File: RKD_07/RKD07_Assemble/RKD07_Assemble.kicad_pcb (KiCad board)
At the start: 2 copper layers, 409.6 x 100 mm, 166 parts, among them J1 Conn_01x02_Socket, J10 Conn_01x04, J11 TRRS, J12 Conn_01x06, J13 Conn_01x06, J2 Conn_01x24, J3 Conn_01x24, J4 Conn_01x24, J5 Qwiic_RA, J6 Qwiic_RA, J7 Conn_01x06, J8 Conn_01x06, J9 Conn_01x04, M3 Mark, M4 Mark, M5 Mark, M6 Mark, M8 Mark, SW1 SW_Push, SW10 SW_Push, SW11 SW_Push, SW12 SW_Push, SW13 SW_Push, SW14 SW_Push, SW15 SW_Push, SW16 SW_Push, SW17 SW_Push, SW18 SW_Push, SW19 SW_Push, SW2 SW_Push, SW20 SW_Push, SW21 SW_Push, SW22 SW_Push, SW23 SW_Push, SW24 SW_Push, SW25 SW_Push, SW26 SW_Push, SW27 SW_Push, SW28 SW_Push, SW29 SW_Push, SW3 SW_Push, SW30 RotaryEncoder_Switch, SW31 SW_Push, SW4 SW_Push, SW5 SW_Push, SW51 SW_Push, SW52 SW_Push, SW53 SW_Push, SW54 SW_Push, SW55 SW_Push, SW56 SW_Push, SW57 SW_Push, SW58 SW_Push, SW59 SW_Push, SW6 SW_Push, SW60 SW_Push, SW61 SW_Push, SW62 SW_Push, SW63 SW_Push, SW64 SW_Push, SW65 SW_Push, SW66 SW_Push, SW67 SW_Push, SW68 SW_Push, SW69 SW_Push, SW7 SW_Push, SW70 SW_Push, SW71 SW_Push, SW72 SW_Push, SW73 SW_Push, SW74 SW_Push, SW75 SW_Push, SW76 SW_Push, SW77 SW_Push, SW78 SW_Push, SW79 SW_Push, SW8 SW_Push, SW80 SW_Push, SW81 SW_Push, SW82 SW_Push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

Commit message: ネジ穴見直し
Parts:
- moved SW31 1.19 mm to (166.7, 188.1)
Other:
- board size 409.6 x 100 mm -> 409.6 x 97.6 mm

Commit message: 07 I2C抵抗追加
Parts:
- removed Ref** (x2): Val**, kbd_Hole:m2_Spacer_Hole_hex
- added R3: R, Resistor_THT:R_Axial_DIN0207_L6.3mm_D2.5mm_P10.16mm_Horizontal, B.Cu at (173.1, 119.6)
- added R4: R, Resistor_THT:R_Axial_DIN0207_L6.3mm_D2.5mm_P10.16mm_Horizontal, B.Cu at (169.1, 119.6)
- SW25, SW4, SW86, SW88: footprint Rikkodo_FootPrint:rkd_Asm_ChocV2_Hotswap_2u -> Rikkodo_FootPrint:rkd_Asm_ChocV2_Hotswap_2uW
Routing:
- net 3v3_L: track 140.2 -> 173.1 mm
- net GND_L: track 241.2 -> 213.1 mm
- net SCL/TX_L: track 145.9 -> 140.4 mm, vias 0 -> 1
- net SCL/TX_R: track 188.9 -> 191.9 mm
- net SDA/SCK_L: track 152.5 -> 155.0 mm, vias 0 -> 1
- net VCC_L: track 23.0 -> 20.9 mm
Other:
- outline, holes or cut-outs redrawn
- board text added: "GND 3V3 SDA SCL"
- board text added: "GND SCK TX MOT CS 3V3"
- board text removed: "SCL/TX"
- board text removed: "SDA/SCK"

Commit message: 07 ワイヤ調整
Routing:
- net 3v3_R: track 254.2 -> 261.9 mm
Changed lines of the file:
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@@
 	(gr_arc
 		(start 248.840625 133.349908)
-		(mid 247.998809 133.001216)
+		(mid 247.998793 133.001225)
 		(end 247.650117 132.1594)
 		(stroke
@@
 	(gr_arc
 		(start 76.199975 94.05935)
-		(mid 76.548716 93.217466)
+		(mid 76.548713 93.217448)
 		(end 77.3906 92.868725)
 		(stroke
@@
 	(gr_arc
 		(start 70.246875 92.86875)
-		(mid 71.088796 93.217454)
+		(mid 71.088828 93.217436)
 		(end 71.4375 94.059375)
 		(stroke
@@
 	(gr_arc
 		(start 4.7625 94.059375)
-		(mid 5.111228 93.217485)
+		(mid 5.11123 93.21748)
 		(end 5.953125 92.86875)
 		(stroke
@@
 	(gr_arc
 		(start 251.209746 133.350138)
-		(mid 252.059665 133.694421)
+		(mid 252.059664 133.694427)
 		(end 252.412712 134.540738)
 		(stroke
@@
 	)
 	(segment
+		(start 256.579903 180.975152)
+		(end 256.579903 157.755547)
+		(width 0.25)
+		(layer "B.Cu")
+		(net 63)
+	)
+	(segment
 		(start 190.75 127.928125)
 		(end 190.75 117.859225)
@@
 	)
 	(segment
-		(start 238.125 186.928125)
-		(end 247.81249 186.928125)
+		(start 259.8042 154.53125)
+		(end 267.37812 154.53125)
 		(width 0.25)
 		(layer "B.Cu")
@@
 	)
 	(segment
-		(start 188.11875 165.80625)
-		(end 195.945625 173.633125)
+		(start 214.135375 186.751)
+		(end 224.177115 186.751)
 		(width 0.25)
 		(layer "B.Cu")
@@
 	)
 	(segment
-		(start 250.788898 183.951717)
-		(end 253.603338 183.951717)
+		(start 188.11875 165.80625)
+		(end 195.945625 173.633125)
 		(width 0.25)
 		(layer "B.Cu")
@@
 	)
 	(segment
-		(start 200.620481 178.91125)
-		(end 203.193606 181.484375)
+		(start 253.603338 183.951717)
+		(end 256.579903 180.975152)
+		(width 0.25)
+		(layer "B.Cu")
+		(net 63)
+	)
+	(segment
+		(start 224.177115 186.751)
+		(end 226.976398 183.951717)
 		(width 0.25)
 		(layer "B.Cu")
@@
 	)
 	(segment
-		(start 226.976398 183.951717)
-		(end 235.148592 183.951717)
+		(start 200.620481 178.91125)
+		(end 203.193606 181.484375)
 		(width 0.25)
 		(layer "B.Cu")
@@
 	)
 	(segment
-		(start 190.75 117.859225)
-		(end 195.249755 113.35947)
+		(start 211.18125 183.796875)
+		(end 214.135375 186.751)
 		(width 0.25)
 		(layer "B.Cu")
@@
 	)
 	(segment
-		(start 256.579903 180.975152)
-		(end 256.579903 157.755547)
+		(start 238.125 186.928125)
+		(end 247.81249 186.928125)
 		(width 0.25)
 		(layer "B.Cu")
@@
 	)
 	(segment
-		(start 203.193606 181.484375)
-		(end 210.740625 181.484375)
+		(start 190.75 117.859225)
+		(end 195.249755 113.35947)
 		(width 0.25)
 		(layer "B.Cu")
@@
 	)
 	(segment
-		(start 190.75 128.932544)
-		(end 190.75 127.928125)
+		(start 203.193606 181.484375)
+		(end 210.740625 181.484375)
 		(width 0.25)
 		(layer "B.Cu")
@@
 	)
 	(segment
-		(start 214.135375 186.751)
-		(end 224.177115 186.751)
+		(start 190.75 128.932544)
+		(end 190.75 127.928125)
 		(width 0.25)
 		(layer "B.Cu")
@@
 	)
 	(segment
-		(start 211.18125 183.796875)
-		(end 214.135375 186.751)
+		(start 247.81249 186.928125)
+		(end 250.788898 183.951717)
 		(width 0.25)
 		(layer "B.Cu")
@@
 	)
 	(segment
-		(start 259.8042 154.53125)
-		(end 267.37812 154.53125)
+		(start 226.976398 183.951717)
+		(end 235.148592 183.951717)
 		(width 0.25)
 		(layer "B.Cu")
@@
 	)
 	(segment
-		(start 247.81249 186.928125)
-		(end 250.788898 183.951717)
+		(start 250.788898 183.951717)
+		(end 253.603338 183.951717)
 		(width 0.25)
 		(layer "B.Cu")
@@
 	)
 	(segment
-		(start 224.177115 186.751)
-		(end 226.976398 183.951717)
-		(width 0.25)
-		(layer "B.Cu")
-		(net 63)
-	)
-	(segment
 		(start 195.945625 173.633125)
 		(end 197.28125 173.633125)
@@
 	)
 	(segment
-		(start 253.603338 183.951717)
-		(end 256.579903 180.975152)
-		(width 0.25)
-		(layer "B.Cu")
-		(net 63)
-	)
-	(segment
 		(start 373.85625 153.0062)
 		(end 392.90625 153.0062)
@@
 	)
 	(segment
-		(start 188.11875 163.80625)
-		(end 187.428125 163.80625)
+		(start 265.950756 175.77149)
+		(end 265.950756 166.813439)
 		(width 0.5)
 		(layer "B.Cu")
@@
 	)
 	(segment
-		(start 265.950756 175.77149)
-		(end 257.175216 184.54703)
-		(width 0.3)
+		(start 188.11875 163.80625)
+		(end 187.428125 163.80625)
+		(width 0.5)
 		(layer "B.Cu")
 		(net 69)
 	)
 	(segment
-		(start 193.464221 108.35947)
-		(end 197.579855 108.35947)
-		(width 0.3)
+		(start 207.44672 187.523595)
+		(end 225.121614 187.523595)
+		(width 0.5)
 		(layer "B.Cu")
 		(net 69)
 	)
 	(segment
-		(start 237.529887 188.11875)
-		(end 233.958167 184.54703)
-		(width 0.3)
+		(start 271.73112 156.13225)
+		(end 267.37812 156.13225)
+		(width 0.5)
 		(layer "B.Cu")
 		(net 69)
 	)
 	(segment
-		(start 252.0521 184.54703)
-		(end 248.48038 188.11875)
-		(width 0.3)
+		(start 251.22172 184.54703)
+		(end 257.175216 184.54703)
+		(width 0.5)
 		(layer "B.Cu")
 		(net 69)
 	)
 	(segment
-		(start 205.978125 186.055)
-		(end 207.44672 187.523595)
+		(start 237.529887 188.11875)
+		(end 247.65 188.11875)
 		(width 0.5)
 		(layer "B.Cu")
@@
 	)
 	(segment
-		(start 233.958167 184.54703)
-		(end 228.004879 184.54703)
+		(start 193.464221 108.35947)
+		(end 197.579855 108.35947)
 		(width 0.3)
 		(layer "B.Cu")
@@
 	)
 	(segment
-		(start 185.75 127.928125)
-		(end 185.75 157.776739)
-		(width 0.3)
+		(start 204.7875 186.055)
+		(end 205.978125 186.055)
+		(width 0.5)
 		(layer "B.Cu")
 		(net 69)
 	)
 	(segment
-		(start 228.004879 184.54703)
-		(end 225.028314 187.523595)
+		(start 185.75 127.928125)
+		(end 185.75 157.776739)
 		(width 0.3)
 		(layer "B.Cu")
@@
 	)
 	(segment
-		(start 204.7875 186.055)
-		(end 205.978125 186.055)
+		(start 234.085137 184.674)
+		(end 237.529887 188.11875)
 		(width 0.5)
 		(layer "B.Cu")
@@
 	)
 	(segment
-		(start 225.028314 187.523595)
-		(end 207.44672 187.523595)
-		(width 0.3)
+		(start 272.17912 163.071185)
+		(end 272.17912 156.58025)
+		(width 0.5)
 		(layer "B.Cu")
 		(net 69)
 	)
 	(segment
-		(start 187.428125 163.80625)
-		(end 185.7375 165.496875)
+		(start 265.950756 166.813439)
+		(end 267.838195 164.926)
 		(width 0.5)
 		(layer "B.Cu")
@@
 	)
 	(segment
-		(start 185.75 127.928125)
-		(end 185.75 116.073691)
-		(width 0.3)
+		(start 187.428125 163.80625)
+		(end 185.7375 165.496875)
+		(width 0.5)
 		(layer "B.Cu")
 		(net 69)
 	)
 	(segment
-		(start 265.98225 157.42712)
-		(end 265.98225 175.77149)
+		(start 185.75 127.928125)
+		(end 185.75 116.073691)
 		(width 0.3)
 		(layer "B.Cu")
@@
 	)
 	(segment
-		(start 185.75 157.776739)
-		(end 196.724511 168.75125)
-		(width 0.3)
+		(start 267.838195 164.926)
+		(end 270.324305 164.926)
+		(width 0.5)
 		(layer "B.Cu")
 		(net 69)
 	)
 	(segment
-		(start 257.175216 184.54703)
-		(end 252.0521 184.54703)
-		(width 0.3)
+		(start 225.121614 187.523595)
+		(end 227.971209 184.674)
+		(width 0.5)
 		(layer "B.Cu")
 		(net 69)
 	)
 	(segment
-		(start 248.48038 188.11875)
-		(end 237.529887 188.11875)
+		(start 185.75 157.776739)
+		(end 196.724511 168.75125)
 		(width 0.3)
 		(layer "B.Cu")
@@
 	)
 	(segment
-		(start 267.37812 156.03125)
-		(end 265.98225 157.42712)
-		(width 0.3)
-		(layer "B.Cu")
-		(net 69)
-	)
-	(segment
 		(start 197.28125 178.713125)
 		(end 197.28125 176.173125)
@@
 	)
 	(segment
-		(start 265.98225 175.77149)
+		(start 227.971209 184.674)
+		(end 234.085137 184.674)
+		(width 0.5)
+		(layer "B.Cu")
+		(net 69)
+	)
+	(segment
+		(start 205.978125 186.055)
+		(end 207.44672 187.523595)
+		(width 0.5)
+		(layer "B.Cu")
+		(net 69)
+	)
+	(segment
+		(start 247.65 188.11875)
+		(end 251.22172 184.54703)
+		(width 0.5)
+		(layer "B.Cu")
+		(net 69)
+	)
+	(segment
+		(start 257.175216 184.54703)
 		(end 265.950756 175.77149)
-		(width 0.3)
+		(width 0.5)
+		(layer "B.Cu")
+		(net 69)
+	)
+	(segment
+		(start 270.324305 164.926)
+		(end 272.17912 163.071185)
+		(width 0.5)
+		(layer "B.Cu")
+		(net 69)
+	)
+	(segment
+		(start 272.17912 156.58025)
+		(end 271.73112 156.13225)
+		(width 0.5)
 		(layer "B.Cu")
 		(net 69)

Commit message: QWICC位置など調整
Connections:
- U1 pad 1: ROW0_L -> DATA
- U1 pad 10: COL4_L -> COL3_L
- U1 pad 11: COL5_L -> COL4_L
- U1 pad 12: DATA -> COL5_L
- U1 pad 2: RE_B -> ROW0_L
- U1 pad 4: COL0_L -> RE_B
- U1 pad 5: COL1_L -> COL0_L
- U1 pad 6: RE_A -> COL1_L
- U1 pad 7: COL2_L -> RE_A
- U1 pad 9: COL3_L -> COL2_L
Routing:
- net DATA: track 51.8 -> 24.2 mm
- net RE_B: track 127.0 -> 122.8 mm
- net RE_A: track 102.3 -> 99.8 mm
- net ROW0_L: track 162.7 -> 160.6 mm
- net COL4_L: track 154.5 -> 156.6 mm
- net COL0_L: track 239.8 -> 237.9 mm
- net COL3_L: track 180.8 -> 182.4 mm
- net ROW3_L: track 170.9 -> 169.5 mm
- net ROW1_L: track 158.0 -> 156.6 mm
- net ROW2_L: track 154.4 -> 153.7 mm

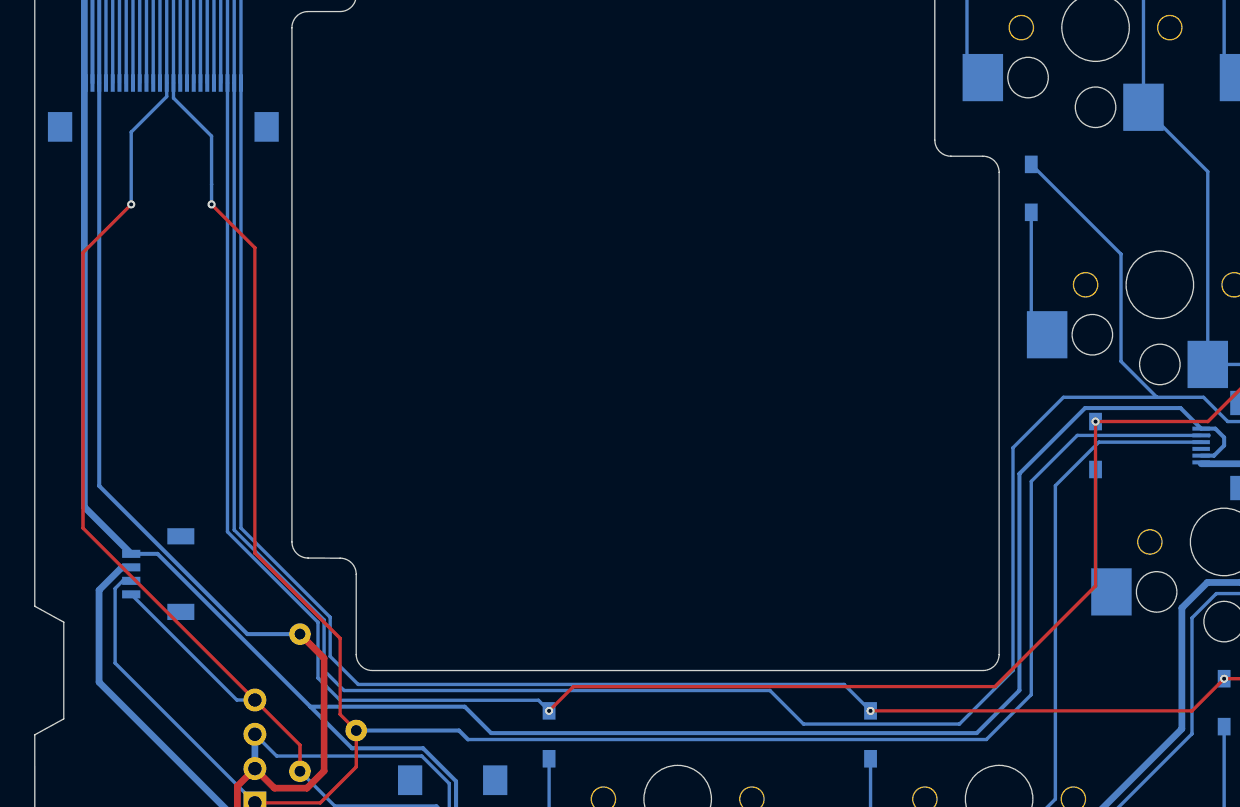
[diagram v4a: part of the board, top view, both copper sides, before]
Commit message: OLED追加
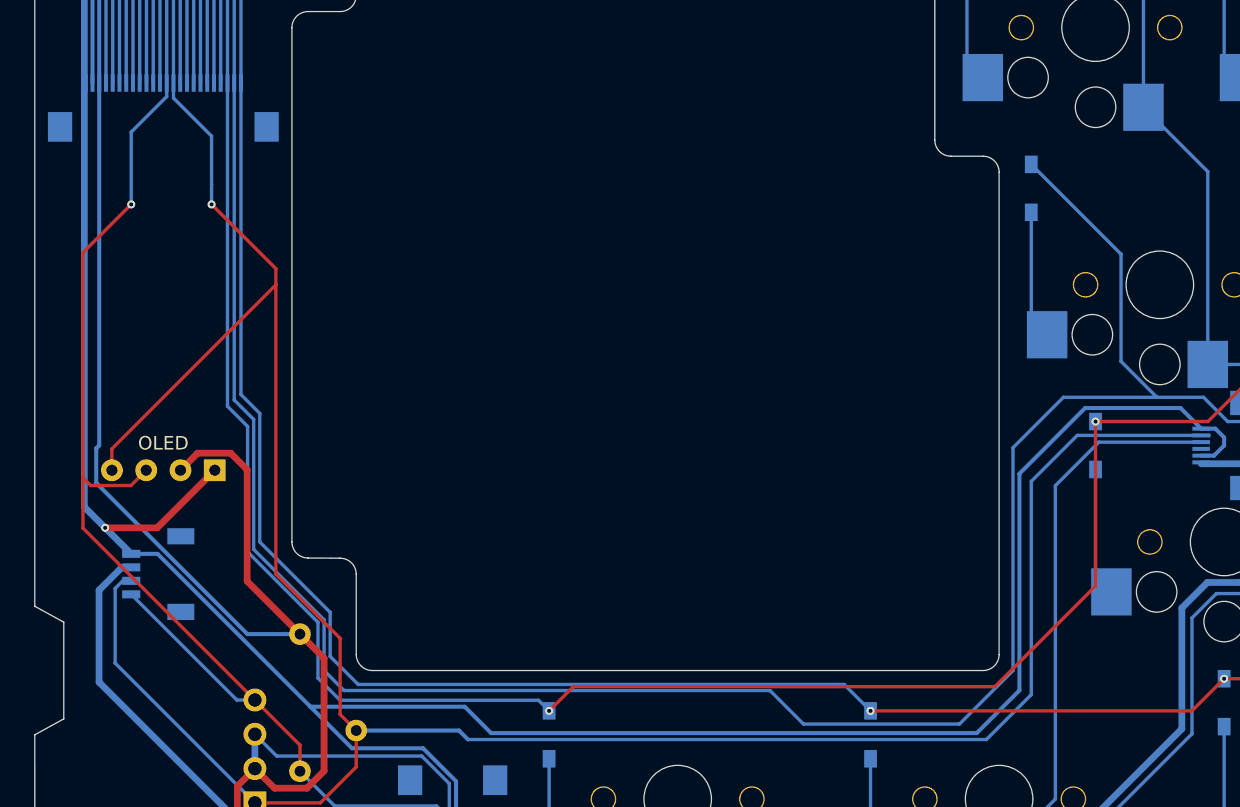
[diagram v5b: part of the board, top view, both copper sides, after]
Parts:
- added OL3: OLED, BrownSugar_KBD:OLED_center_display, F.Cu at (190.5, 138.1)
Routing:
- net 3v3_R: track 261.9 -> 281.9 mm
- net SDA/SCK_R: track 200.0 -> 218.8 mm
- net GND_R: track 191.2 -> 201.1 mm, vias 0 -> 1
- net SCL/TX_R: track 191.9 -> 197.3 mm

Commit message: Modify for SekiBall
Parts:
- removed Point1: Guard_Screw_Hall, Rikkodo_FootPrint:rkd_Guard_Screw_Hall
- added J14: Conn_01x02_Socket, Connector_PinHeader_2.54mm:PinHeader_1x02_P2.54mm_Horizontal, B.Cu at (133.9, 118.7)
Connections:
- J11 pad B: unconnected-(J11-PadB) -> UART_TX/SCK_L
- J11 pad C: DATA -> UART_RX/TX_L
- J8 pad 2: SCK_L -> UART_TX/SCK_L
- J8 pad 3: TX_L -> UART_RX/TX_L
- J8 pad 5: GND_L -> CS/GND
- U1 pad 1: DATA -> UART_TX/SCK_L
- U1 pad 10: COL3_L -> RE_B
- U1 pad 11: COL4_L -> COL2_L
- U1 pad 12: COL5_L -> COL3_L
- U1 pad 14: ROW1_L -> COL4_L
- U1 pad 15: ROW2_L -> COL5_L
- U1 pad 16: ROW3_L -> ROW1_L
- U1 pad 17: ROW4_L -> ROW2_L
- U1 pad 19: SCK_L -> ROW3_L
- U1 pad 2: ROW0_L -> UART_RX/TX_L
- U1 pad 20: TX_L -> ROW4_L
- U1 pad 3: unconnected-(U1-GND-Pad3) -> GND_L
- U1 pad 4: RE_B -> CS/GND
- U1 pad 5: COL0_L -> ROW0_L
- U1 pad 6: COL1_L -> RE_A
- U1 pad 7: RE_A -> COL0_L
- U1 pad 9: COL2_L -> COL1_L
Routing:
- net UART_TX/SCK_L: track 0.00 -> 91.2 mm, vias 0 -> 1
- net UART_RX/TX_L: track 0.00 -> 88.1 mm, vias 0 -> 1
- net CS/GND: track 0.00 -> 80.2 mm, vias 0 -> 1
- net GND_L: track 213.1 -> 240.2 mm
- net DATA: track 24.2 -> 0.00 mm
- net SCK_L: track 23.8 -> 0.00 mm
- net ROW4_L: track 199.4 -> 217.4 mm
- net TX_L: track 16.2 -> 0.00 mm
- net RE_B: track 122.8 -> 112.2 mm
- net COL4_L: track 156.6 -> 165.7 mm
- net RE_A: track 99.8 -> 108.7 mm
- net ROW1_L: track 156.6 -> 163.7 mm
- net 3v3_L: track 173.1 -> 166.2 mm
- net COL3_L: track 182.4 -> 187.0 mm
- net COL5_L: track 140.8 -> 145.3 mm
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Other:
- board text added: "3V3 CS MOT TX SCK GND"
- board text added: "CS/HandDetect"
- board text added: "GND"

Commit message: RKD07 調整
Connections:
- U1 pad 34: COL13_L -> ROW0_L
- U1 pad 5: ROW0_L -> COL13_L
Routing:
- net ROW0_L: track 156.7 -> 164.3 mm
- net COL13_L: track 7.38 -> 12.5 mm
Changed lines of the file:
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@@
 			(layers "*.Cu" "*.Mask")
 			(remove_unused_layers no)
-			(net 51 "ROW0_L")
+			(net 130 "COL13_L")
 			(pinfunction "GPIO3")
 			(pintype "bidirectional")
@@
 			(layers "*.Cu" "*.Mask")
 			(remove_unused_layers no)
-			(net 130 "COL13_L")
+			(net 51 "ROW0_L")
 			(pinfunction "GPIO28_ADC2")
 			(pintype "bidirectional")
@@
 	)
 	(segment
-		(start 102.39375 95.8562)
-		(end 133.56145 95.8562)
+		(start 156.63125 108.859375)
+		(end 162.358125 108.859375)
 		(width 0.25)
 		(layer "B.Cu")
@@
 	)
 	(segment
-		(start 149.658125 108.859375)
-		(end 156.63125 108.859375)
+		(start 146.646375 101.3765)
+		(end 154.12925 108.859375)
 		(width 0.25)
 		(layer "B.Cu")
@@
 	)
 	(segment
-		(start 145.89125 105.0925)
-		(end 149.658125 108.859375)
+		(start 162.358125 108.859375)
+		(end 163.67125 110.1725)
+		(width 0.25)
+		(layer "B.Cu")
+		(net 51)
+	)
+	(segment
+		(start 102.39375 95.8562)
+		(end 133.56145 95.8562)
 		(width 0.25)
 		(layer "B.Cu")
@@
 	)
 	(segment
-		(start 145.89125 105.0925)
-		(end 142.79775 105.0925)
+		(start 7.14375 95.8562)
+		(end 26.19375 95.8562)
 		(width 0.25)
 		(layer "B.Cu")
@@
 	)
 	(segment
-		(start 7.14375 95.8562)
-		(end 26.19375 95.8562)
+		(start 133.56145 95.8562)
+		(end 139.08175 101.3765)
 		(width 0.25)
 		(layer "B.Cu")
@@
 	)
 	(segment
-		(start 142.79775 105.0925)
-		(end 133.56145 95.8562)
+		(start 154.12925 108.859375)
+		(end 156.63125 108.859375)
 		(width 0.25)
 		(layer "B.Cu")
@@
 	)
 	(segment
+		(start 139.08175 101.3765)
+		(end 146.646375 101.3765)
+		(width 0.25)
+		(layer "B.Cu")
+		(net 51)
+	)
+	(segment
 		(start 77.774551 95.8562)
 		(end 83.34375 95.8562)
@@
 	)
 	(segment
-		(start 156.63125 109.359375)
-		(end 162.858125 109.359375)
+		(start 145.89125 105.0925)
+		(end 150.158125 109.359375)
 		(width 0.25)
 		(layer "B.Cu")
@@
 	)
 	(segment
-		(start 162.858125 109.359375)
-		(end 163.67125 110.1725)
+		(start 150.158125 109.359375)
+		(end 156.63125 109.359375)
 		(width 0.25)
 		(layer "B.Cu")
